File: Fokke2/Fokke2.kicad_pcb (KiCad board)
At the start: 2 copper layers, 220 x 61.5 mm, 55 parts, among them J1 Conn_01x20_Male, SW1 SW_SPST, SW2 SW_SPST, SW3 SW_SPST, SW4 SW_SPST, SW5 SW_SPST, SW6 SW_SPST, SW7 SW_SPST, SW8 SW_SPST, SW9 SW_SPST

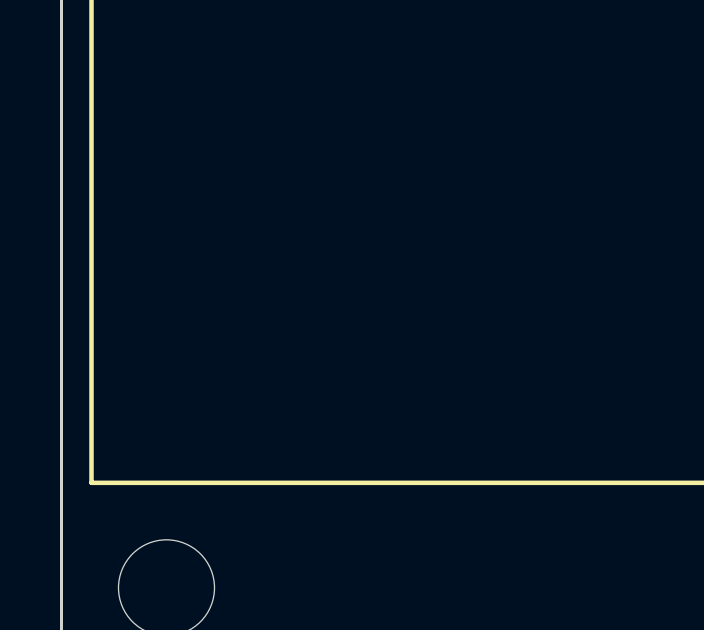
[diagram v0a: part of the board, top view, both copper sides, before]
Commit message: added logo and layout plans
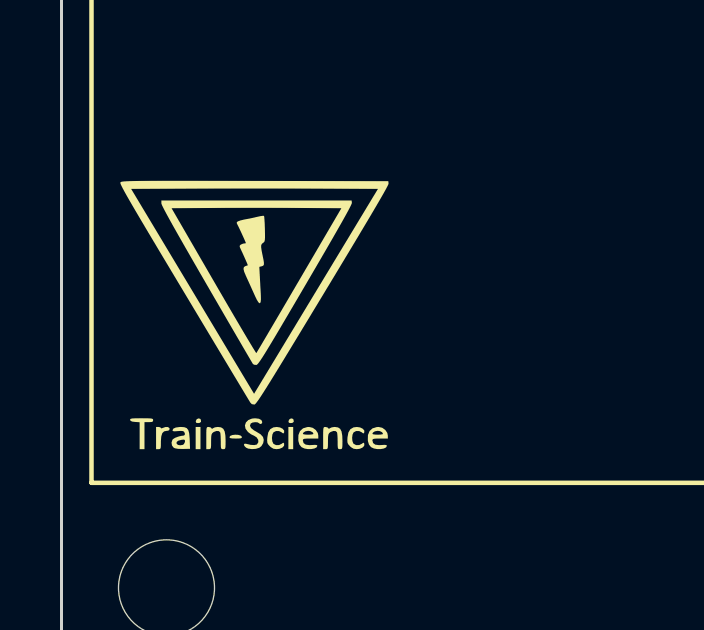
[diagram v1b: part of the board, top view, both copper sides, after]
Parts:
- added G***: LOGO, kicad_images:Train-Science logo small, F.Cu at (36.5, 110.0)

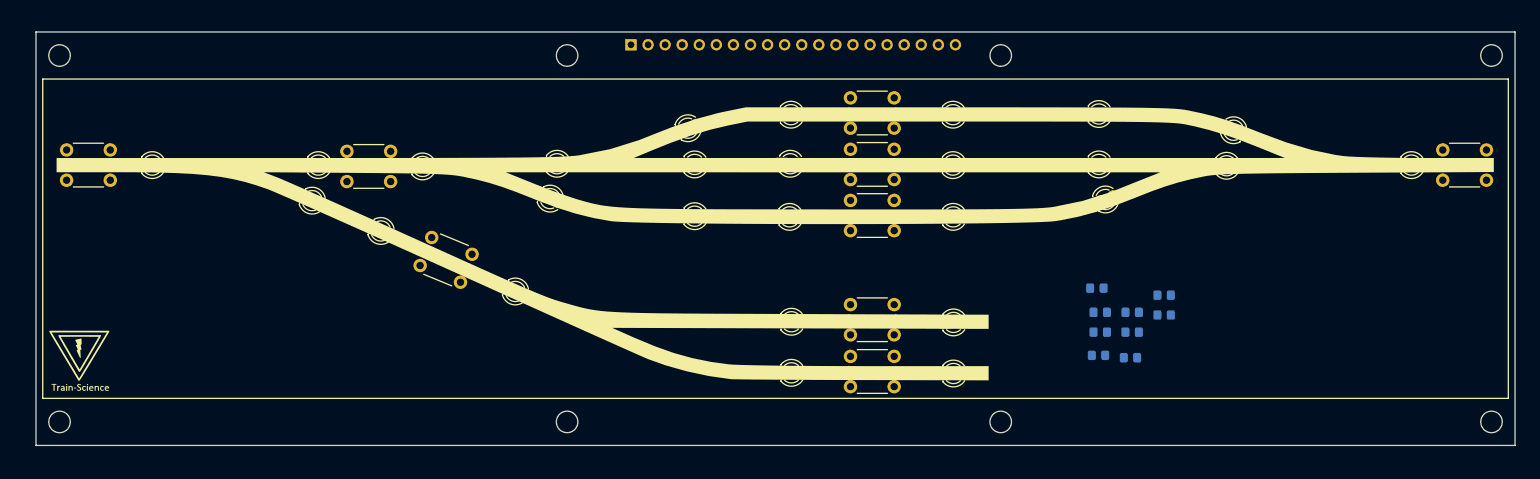
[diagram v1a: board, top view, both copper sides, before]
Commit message: did alot of work on Fokke2. The connector is still needed. Also going to make a module flatcable controller line
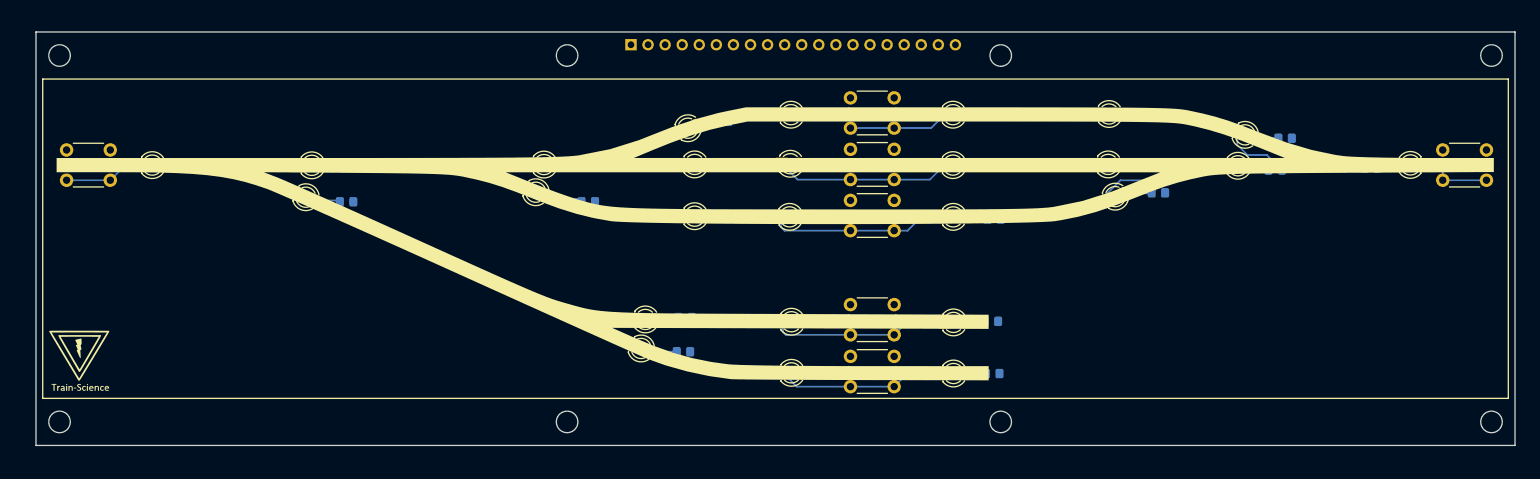
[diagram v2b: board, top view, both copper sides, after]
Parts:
- removed D2 (x2), D3 (x3): LED, LED_THT:LED_D3.0mm
- removed R2, R3, R4, R5, R6, R8, R9: R, Resistor_SMD:R_0805_2012Metric_Pad1.20x1.40mm_HandSolder
- removed the SW2 at (76.2, 78.8)
- removed the SW3 at (88.9, 91.6)
- added D101: LED, LED_THT:LED_D3.0mm, F.Cu at (119.4, 103.8)
- added D102: LED, LED_THT:LED_D3.0mm, F.Cu at (118.8, 107.6)
- added D81: LED, LED_THT:LED_D3.0mm, F.Cu at (69.0, 85.1)
- added D82: LED, LED_THT:LED_D3.0mm, F.Cu at (69.8, 80.8)
- added R101: R, Resistor_SMD:R_0805_2012Metric_Pad1.20x1.40mm_HandSolder, B.Cu at (126.5, 103.5)
- added R102: R, Resistor_SMD:R_0805_2012Metric_Pad1.20x1.40mm_HandSolder, B.Cu at (126.3, 108.6)
- added R111: R, Resistor_SMD:R_0805_2012Metric_Pad1.20x1.40mm_HandSolder, B.Cu at (132.0, 74.3)
- added R112: R, Resistor_SMD:R_0805_2012Metric_Pad1.20x1.40mm_HandSolder, B.Cu at (133.4, 80.7)
- added R121: R, Resistor_SMD:R_0805_2012Metric_Pad1.20x1.40mm_HandSolder, B.Cu at (197.0, 84.9)
- added R122: R, Resistor_SMD:R_0805_2012Metric_Pad1.20x1.40mm_HandSolder, B.Cu at (196.6, 80.7)
- added R131: R, Resistor_SMD:R_0805_2012Metric_Pad1.20x1.40mm_HandSolder, B.Cu at (215.8, 76.8)
- added R132: R, Resistor_SMD:R_0805_2012Metric_Pad1.20x1.40mm_HandSolder, B.Cu at (214.3, 81.5)
- added R21: R, Resistor_SMD:R_0805_2012Metric_Pad1.20x1.40mm_HandSolder, B.Cu at (147.1, 73.4)
- added R22: R, Resistor_SMD:R_0805_2012Metric_Pad1.20x1.40mm_HandSolder, B.Cu at (172.1, 73.3)
- added R23: R, Resistor_SMD:R_0805_2012Metric_Pad1.20x1.40mm_HandSolder, B.Cu at (194.6, 73.2)
- added R31: R, Resistor_SMD:R_0805_2012Metric_Pad1.20x1.40mm_HandSolder, B.Cu at (147.1, 80.8)
- added R32: R, Resistor_SMD:R_0805_2012Metric_Pad1.20x1.40mm_HandSolder, B.Cu at (172.3, 81.1)
- added R41: R, Resistor_SMD:R_0805_2012Metric_Pad1.20x1.40mm_HandSolder, B.Cu at (132.8, 88.4)
- added R42: R, Resistor_SMD:R_0805_2012Metric_Pad1.20x1.40mm_HandSolder, B.Cu at (147.2, 88.4)
- added R43: R, Resistor_SMD:R_0805_2012Metric_Pad1.20x1.40mm_HandSolder, B.Cu at (172.5, 88.8)
- added R51: R, Resistor_SMD:R_0805_2012Metric_Pad1.20x1.40mm_HandSolder, B.Cu at (147.4, 104.1)
- added R52: R, Resistor_SMD:R_0805_2012Metric_Pad1.20x1.40mm_HandSolder, B.Cu at (172.1, 104.0)
- added R61: R, Resistor_SMD:R_0805_2012Metric_Pad1.20x1.40mm_HandSolder, B.Cu at (147.4, 111.9)
- added R62: R, Resistor_SMD:R_0805_2012Metric_Pad1.20x1.40mm_HandSolder, B.Cu at (172.3, 111.8)
- added R81: R, Resistor_SMD:R_0805_2012Metric_Pad1.20x1.40mm_HandSolder, B.Cu at (76.2, 86.3)
- added R82: R, Resistor_SMD:R_0805_2012Metric_Pad1.20x1.40mm_HandSolder, B.Cu at (77.0, 80.9)
- added R91: R, Resistor_SMD:R_0805_2012Metric_Pad1.20x1.40mm_HandSolder, B.Cu at (112.2, 86.3)
- added R92: R, Resistor_SMD:R_0805_2012Metric_Pad1.20x1.40mm_HandSolder, B.Cu at (112.0, 80.6)
- moved R1 137.6 mm to (53.0, 80.9)
- moved R7 44.5 mm to (228.6, 81.3), turned to 0 degrees
- moved D7 2.39 mm to (235.7, 80.8), turned to 180 degrees
- moved D91 2.34 mm to (103.2, 84.3)
- moved D92 1.94 mm to (104.3, 80.7)
- moved D132 1.69 mm to (207.5, 80.9)
- moved D121 1.52 mm to (189.4, 86.0)
- moved D23 1.51 mm to (188.3, 73.2)
- moved D122 1.39 mm to (188.2, 80.7)
- moved D131 0.69 mm to (208.7, 75.8), turned to -22.5 degrees
- renumbered D4 to D111, D4 to D112, D4 to D121, D4 to D122, D4 to D131, D4 to D132, D6 to D21, D4 to D22, D6 to D23, D6 to D31, D5 to D32, D6 to D41, D6 to D42, D6 to D43, D7 to D51, D7 to D52, D8 to D61, D8 to D62, D9 to D7, D3 to D91, D4 to D92, SW4 to SW2, SW5 to SW3, SW6 to SW4, SW7 to SW5, SW8 to SW6, SW9 to SW7
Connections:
- D111 pad 1: (no net) -> GPIO11
- D111 pad 2: (no net) -> Net-(R111-Pad2)
- D112 pad 1: (no net) -> GND
- D112 pad 2: (no net) -> Net-(R112-Pad2)
- D121 pad 1: (no net) -> GPIO12
- D121 pad 2: (no net) -> Net-(R121-Pad2)
- D122 pad 1: (no net) -> GND
- D122 pad 2: (no net) -> Net-(R122-Pad2)
- D131 pad 1: (no net) -> GPIO13
- D131 pad 2: (no net) -> Net-(R131-Pad2)
- D132 pad 1: (no net) -> GND
- D132 pad 2: (no net) -> Net-(R132-Pad2)
- D21 pad 1: (no net) -> GPIO2
- D21 pad 2: (no net) -> Net-(D21-Pad2)
- D22 pad 1: GPIO4 -> GPIO2
- D23 pad 1: (no net) -> GPIO2
- D23 pad 2: (no net) -> Net-(R23-Pad2)
- D31 pad 1: (no net) -> GPIO3
- D31 pad 2: (no net) -> Net-(D31-Pad2)
- D32 pad 1: GPIO5 -> GPIO3
- D41 pad 1: (no net) -> GPIO4
- D41 pad 2: (no net) -> Net-(R41-Pad2)
- D42 pad 1: (no net) -> GPIO4
- D42 pad 2: (no net) -> Net-(R42-Pad2)
- D43 pad 1: GPIO6 -> GPIO4
- D51 pad 1: GPIO7 -> GPIO5
- D51 pad 2: Net-(D7-Pad2) -> Net-(D51-Pad2)
- D52 pad 1: GPIO7 -> GPIO5
- D52 pad 2: Net-(D7-Pad2) -> Net-(R52-Pad2)
- D61 pad 1: GPIO8 -> GPIO6
- D61 pad 2: Net-(D8-Pad2) -> Net-(D61-Pad2)
- D62 pad 1: GPIO8 -> GPIO6
- D62 pad 2: Net-(D8-Pad2) -> Net-(R62-Pad2)
- D7 pad 1: GPIO9 -> GPIO7
- D7 pad 2: Net-(D9-Pad2) -> Net-(D7-Pad2)
- D91 pad 1: (no net) -> GPIO9
- D91 pad 2: (no net) -> Net-(R91-Pad2)
- D92 pad 1: (no net) -> GND
- D92 pad 2: (no net) -> Net-(R92-Pad2)
- R1 pad 1: +5V -> +3V3
- R7 pad 1: +5V -> +3V3
- SW2 pad 2: GPIO4 -> GPIO2
- SW3 pad 2: GPIO5 -> GPIO3
- SW4 pad 2: GPIO6 -> GPIO4
- SW5 pad 2: GPIO7 -> GPIO5
- SW6 pad 2: GPIO8 -> GPIO6
- SW7 pad 2: GPIO9 -> GPIO7
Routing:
- net GPIO4: track 0.00 -> 26.9 mm
- net GPIO5: track 0.00 -> 26.6 mm
- net GPIO3: track 0.00 -> 26.1 mm
- net GPIO6: track 0.00 -> 25.8 mm
- net GPIO2: track 0.00 -> 14.8 mm
- net GPIO1: track 0.00 -> 12.4 mm
- net GPIO12: track 0.00 -> 12.0 mm
- net GPIO7: track 0.00 -> 12.0 mm
- net GPIO13: track 0.00 -> 10.2 mm
- net Net-(R91-Pad2): track 0.00 -> 6.03 mm
- net Net-(R122-Pad2): track 0.00 -> 4.85 mm
- net Net-(R121-Pad2): track 0.00 -> 4.28 mm
- net Net-(R92-Pad2): track 0.00 -> 4.26 mm
- net Net-(R102-Pad2): track 0.00 -> 4.12 mm
- net Net-(R81-Pad2): track 0.00 -> 3.97 mm
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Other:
- board text added: "1"
- board text added: "2"
- board text added: "3"
- board text added: "4"
- board text added: "5"
- board text added: "6"
- board text added: "7"

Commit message: I added a button to Fokke 1 for his gate, but I lost annonation with the schematic. The schematic as is now is FUBAR. The project however is finished so I got lucky...
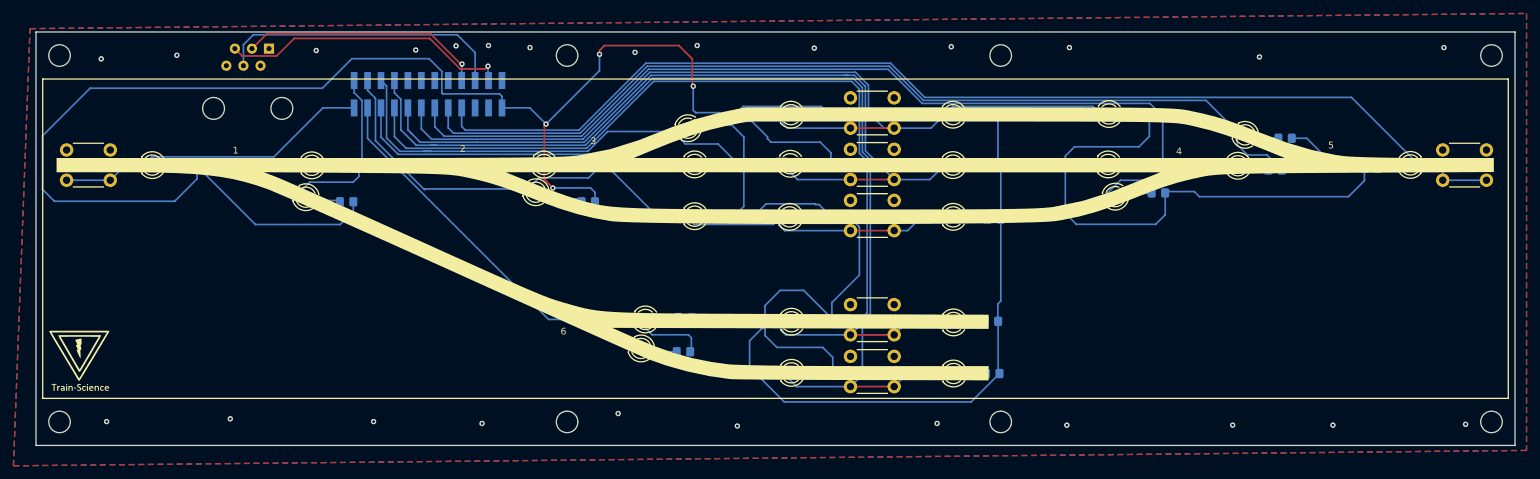
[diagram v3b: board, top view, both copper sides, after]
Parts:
- removed J1: Conn_01x20_Male, Connector_PinHeader_2.54mm:PinHeader_1x20_P2.54mm_Vertical
- added J101: 6P6C, Connector_RJ:RJ12_Amphenol_54601, B.Cu at (64.7, 63.5)
- added J102: panelX_controller, custom_kicad_lib_sk:panelX_contoller, B.Cu at (89.5, 79.6)
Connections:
- D101 pad 1: GPIO10 -> GPIO3
- D111 pad 1: GPIO11 -> GPIO6
- D121 pad 1: GPIO12 -> GPIO11
- D131 pad 1: GPIO13 -> GPIO12
- D21 pad 1: GPIO2 -> GPIO10
- D22 pad 1: GPIO2 -> GPIO10
- D23 pad 1: GPIO2 -> GPIO10
- D31 pad 1: GPIO3 -> GPIO9
- D32 pad 1: GPIO3 -> GPIO9
- D41 pad 1: GPIO4 -> GPIO5
- D42 pad 1: GPIO4 -> GPIO5
- D43 pad 1: GPIO4 -> GPIO5
- D51 pad 1: GPIO5 -> GPIO7
- D52 pad 1: GPIO5 -> GPIO7
- D61 pad 1: GPIO6 -> GPIO8
- D62 pad 1: GPIO6 -> GPIO8
- D7 pad 1: GPIO7 -> GPIO13
- D81 pad 1: GPIO8 -> GPIO2
- D91 pad 1: GPIO9 -> GPIO4
- R102 pad 1: GPIO10 -> GPIO3
- R112 pad 1: GPIO11 -> GPIO6
- R122 pad 1: GPIO12 -> GPIO11
- R132 pad 1: GPIO13 -> GPIO12
- R82 pad 1: GPIO8 -> GPIO2
- R92 pad 1: GPIO9 -> GPIO4
- SW2 pad 2: GPIO2 -> GPIO10
- SW3 pad 2: GPIO3 -> GPIO9
- SW4 pad 2: GPIO4 -> GPIO5
- SW5 pad 2: GPIO5 -> GPIO7
- SW6 pad 2: GPIO6 -> GPIO8
- SW7 pad 2: GPIO7 -> GPIO13
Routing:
- net +3V3: track 0.00 -> 530.9 mm, vias 0 -> 4
- net GPIO13: track 10.2 -> 167.8 mm
- net GPIO8: track 0.00 -> 154.7 mm
- net GPIO11: track 0.00 -> 137.9 mm
- net GPIO10: track 0.00 -> 134.7 mm
- net GPIO7: track 12.0 -> 143.4 mm
- net GPIO12: track 12.0 -> 139.0 mm
- net GPIO9: track 0.00 -> 119.2 mm
- net GPIO5: track 26.6 -> 96.6 mm
- net Net-(J101-Pad4): track 0.00 -> 43.4 mm
- net +12V: track 0.00 -> 43.4 mm, vias 0 -> 1
- net GPIO6: track 25.8 -> 67.0 mm
- net GPIO3: track 26.1 -> 67.1 mm
- net Net-(J101-Pad3): track 0.00 -> 36.5 mm, vias 0 -> 1
- net GPIO1: track 12.4 -> 47.2 mm
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- added copper zone on B.Cu, net GND
- added copper zone on F.Cu, net GND
